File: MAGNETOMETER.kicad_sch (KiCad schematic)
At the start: 0 parts

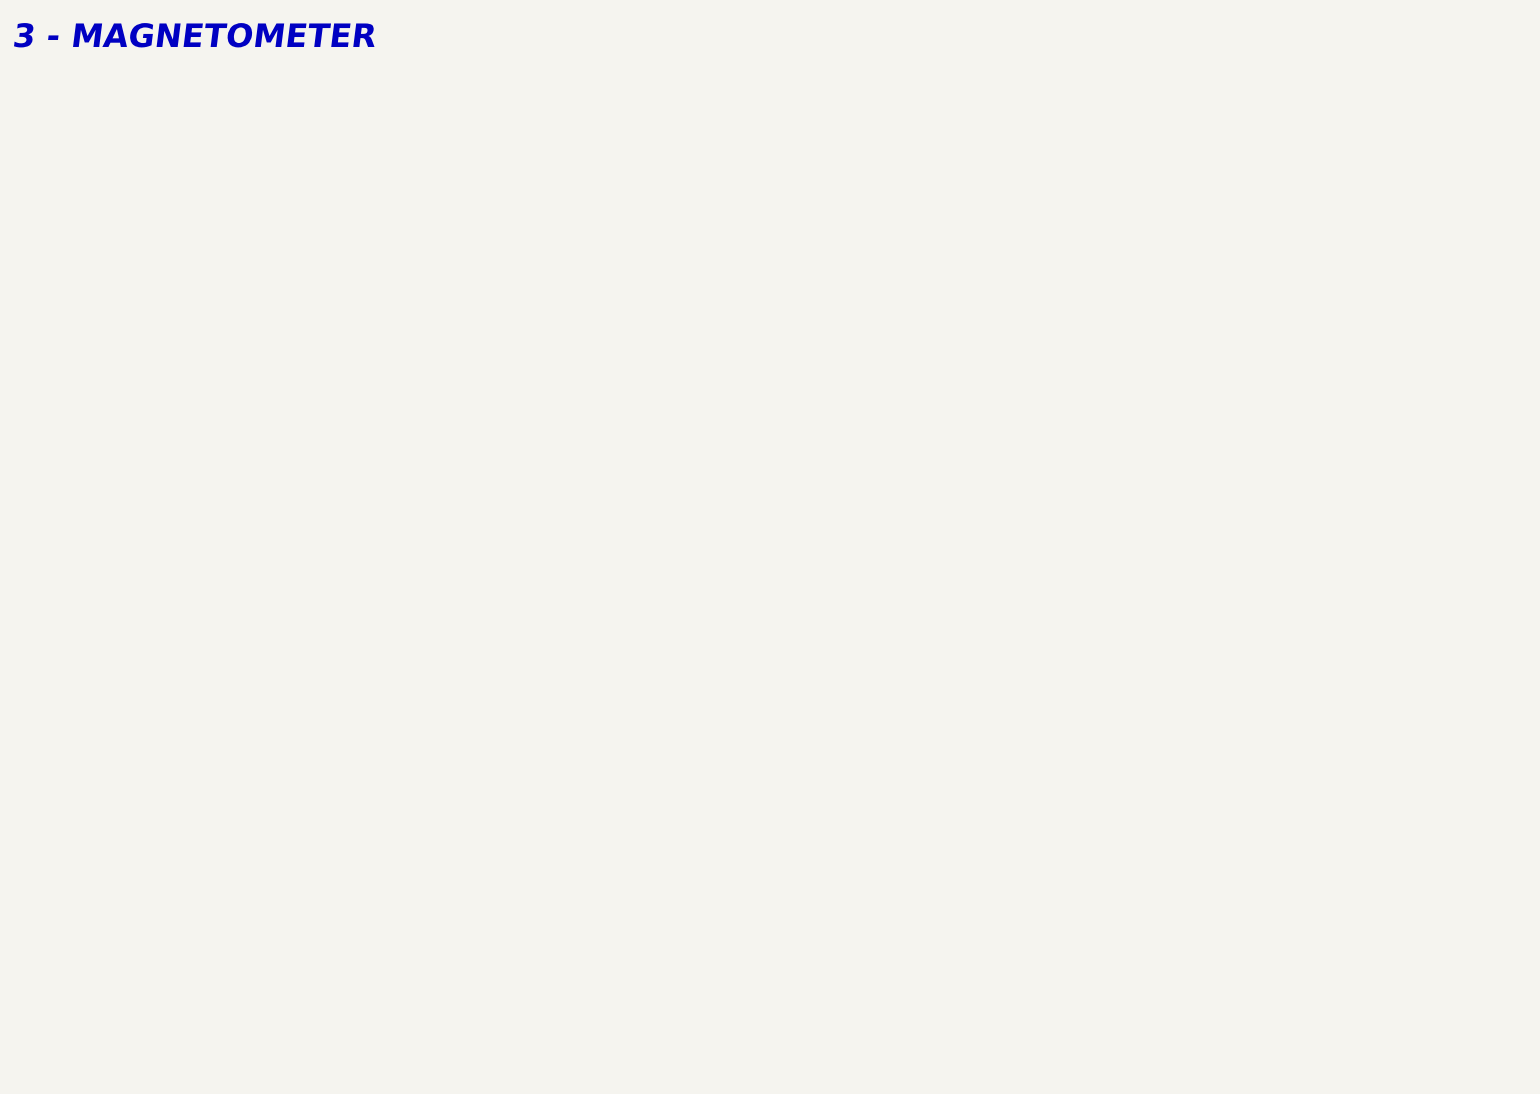
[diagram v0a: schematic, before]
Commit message: magnetometer design
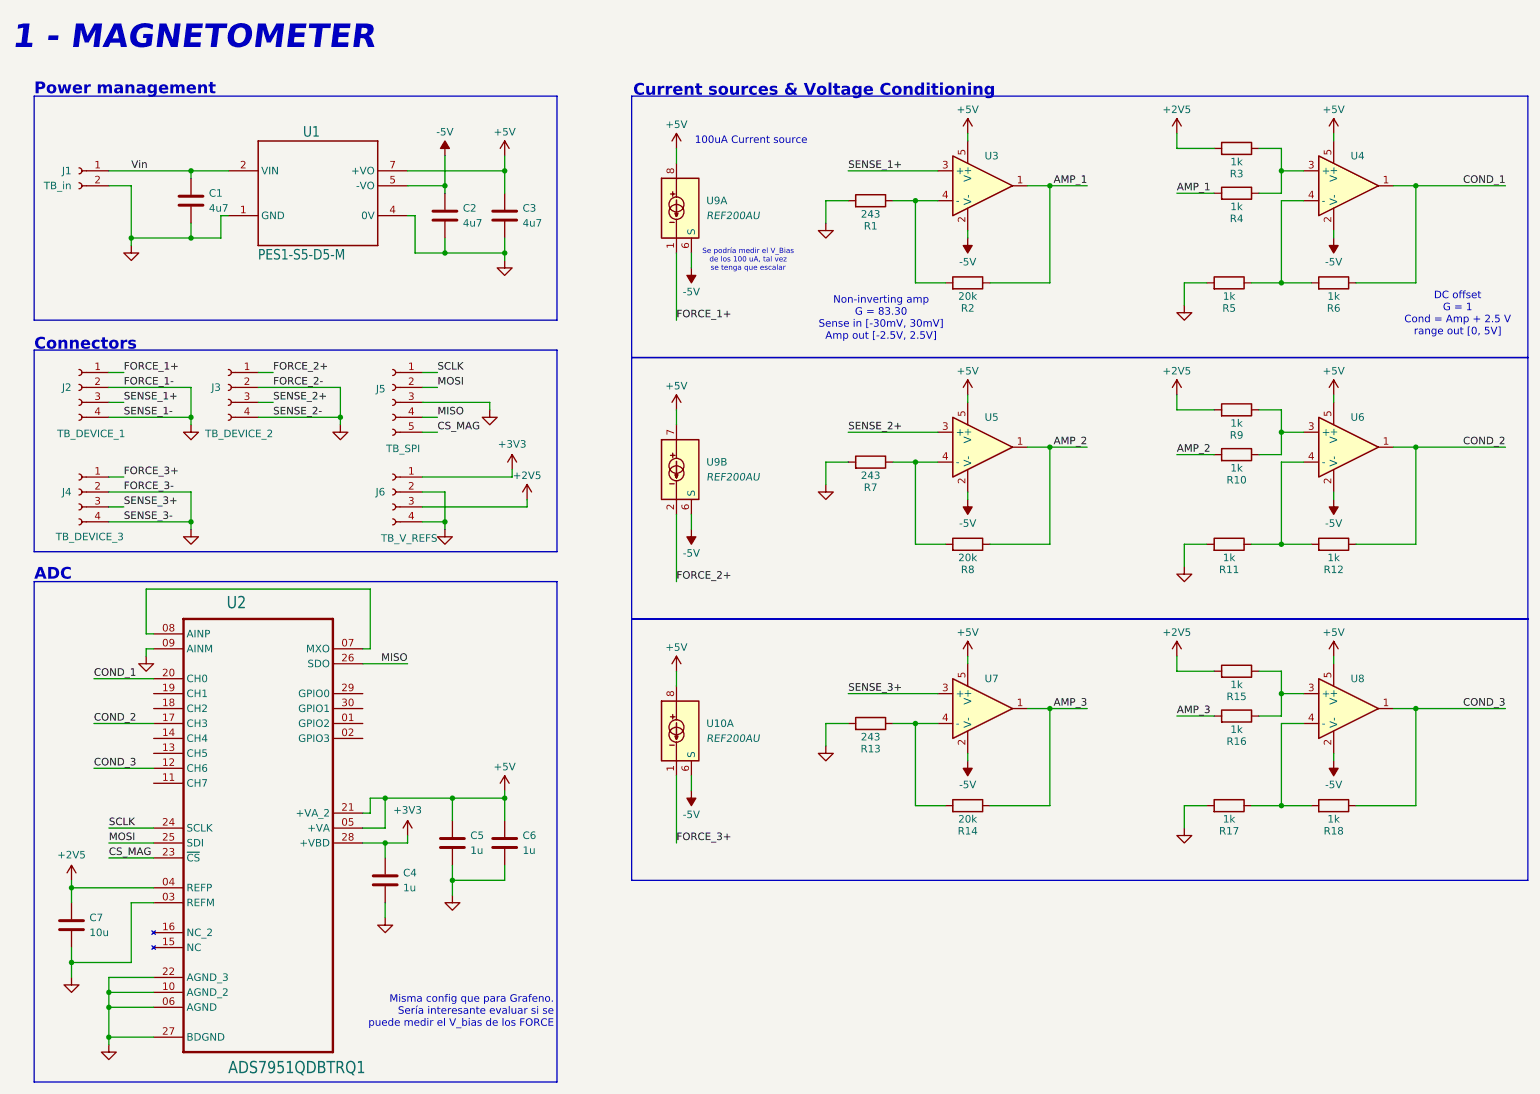
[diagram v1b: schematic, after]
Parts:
- added C1, C2, C3: 4u7, Capacitor_SMD:C_0805_2012Metric_Pad1.18x1.45mm_HandSolder, symbol Device:C
- added C4, C5, C6: 1u, Capacitor_SMD:C_0805_2012Metric_Pad1.18x1.45mm_HandSolder, symbol Device:C
- added C7: 10u, Capacitor_SMD:C_0805_2012Metric_Pad1.18x1.45mm_HandSolder, symbol Device:C
- added J1: TB_in, symbol Connector:Conn_01x02_Socket
- added J2: TB_DEVICE_1, symbol Connector:Conn_01x04_Socket
- added J3: TB_DEVICE_2, symbol Connector:Conn_01x04_Socket
- added J4: TB_DEVICE_3, symbol Connector:Conn_01x04_Socket
- added J5: TB_SPI, symbol Connector:Conn_01x05_Socket
- added J6: TB_V_REFS, symbol Connector:Conn_01x04_Socket
- added R1, R13, R7: 243, Resistor_SMD:R_0805_2012Metric_Pad1.20x1.40mm_HandSolder, symbol Device:R
- added R10, R11, R12, R15, R16, R17, R18, R3, R4, R5, R6, R9: 1k, Resistor_SMD:R_0805_2012Metric_Pad1.20x1.40mm_HandSolder, symbol Device:R
- added R14, R2, R8: 20k, Resistor_SMD:R_0805_2012Metric_Pad1.20x1.40mm_HandSolder, symbol Device:R
- added U1: PES1-S5-D5-M, TG_SAT_24V0_V1.4:CONV_PES1-S5-D24-M, symbol TG_SAT_24V0_V1.4-eagle-import:PES1-S5-D24-M
- added U10, U9: REF200AU, Package_SO:SOIC-8_3.9x4.9mm_P1.27mm, symbol Reference_Current:REF200AU
- added U2: ADS7951QDBTRQ1, Package_SO:TSSOP-30_4.4x7.8mm_P0.5mm, symbol TG_SAT_24V0_V1.4-eagle-import:ADS7951QDBTRQ1
- added U3, U4, U5, U6, U7, U8: ~, Package_TO_SOT_SMD:SOT-23-5_HandSoldering, symbol magnetometer_symbols:OPA189IDBVT
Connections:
- new net: R13.1, R14.2, U7.4 (-)
- new net: R3.1, R4.1, U4.3 (+)
- new net: R5.1, R6.2, U4.4 (-)
- new net: R10.1, R9.1, U6.3 (+)
- new net: R17.1, R18.2, U8.4 (-)
- new net: R11.1, R12.2, U6.4 (-)
- new net: U2.07 (MXO), U2.08 (AINP)
- new net: R7.1, R8.2, U5.4 (-)
- new net: R15.1, R16.1, U8.3 (+)
- new net: R1.1, R2.2, U3.4 (-)
- new net +2V5: C7.1, J6.3 (Pin_3), R15.2, R3.2, R9.2, U2.04 (REFP)
- new net +3V3: C4.1, J6.1 (Pin_1), U2.28 (+VBD)
- new net +5V: C3.1, C5.1, C6.1, U1.7 (+VO), U10.8, U2.05 (+VA), U2.21 (+VA_2), U3.5 (V+), U4.5 (V+), U5.5 (V+), U6.5 (V+), U7.5 (V+), U8.5 (V+), U9.7, U9.8
- new net -5V: C2.1, U1.5 (-VO), U10.6 (S), U3.2 (V-), U4.2 (V-), U5.2 (V-), U6.2 (V-), U7.2 (V-), U8.2 (V-), U9.6 (S), U9.6 (S)
- new net AMP_1: R2.1, R4.2, U3.1
- new net AMP_2: R10.2, R8.1, U5.1
- new net AMP_3: R14.1, R16.2, U7.1
- new net COND_1: R6.1, U2.20 (CH0), U4.1
- new net COND_2: R12.1, U2.17 (CH3), U6.1
- new net COND_3: R18.1, U2.12 (CH6), U8.1
- new net CS_MAG: J5.5 (Pin_5), U2.23 (~{CS})
- new net FORCE_1+: J2.1 (Pin_1), U9.1
- new net FORCE_2+: J3.1 (Pin_1), U9.2
- new net FORCE_3+: J4.1 (Pin_1), U10.1
- new net GND: C1.2, C2.2, C3.2, C4.2, C5.2, C6.2, C7.2, J1.2 (Pin_2), J2.2 (Pin_2), J2.4 (Pin_4), J3.2 (Pin_2), J3.4 (Pin_4), J4.2 (Pin_2), J4.4 (Pin_4), J5.3 (Pin_3), J6.2 (Pin_2), J6.4 (Pin_4), R1.2, R11.2, R13.2, R17.2, R5.2, R7.2, U1.1 (GND), U1.4 (0V), U2.03 (REFM), U2.06 (AGND), U2.09 (AINM), U2.10 (AGND_2), U2.22 (AGND_3), U2.27 (BDGND)
- new net MISO: J5.4 (Pin_4), U2.26 (SDO)
- new net MOSI: J5.2 (Pin_2), U2.25 (SDI)
- new net SCLK: J5.1 (Pin_1), U2.24 (SCLK)
- new net SENSE_1+: J2.3 (Pin_3), U3.3 (+)
- new net SENSE_2+: J3.3 (Pin_3), U5.3 (+)
- new net SENSE_3+: J4.3 (Pin_3), U7.3 (+)
- new net Vin: C1.1, J1.1 (Pin_1), U1.2 (VIN)
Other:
- note added: "1 - MAGNETOMETER"
- note added: "100uA Current source"
- note added: "ADC"
- note added: "Connectors"
- note added: "Current sources & Voltage Conditioning"
- note added: "DC offset G = 1 Cond = Amp + 2.5 V range out [0, 5V]"
- note added: "Misma config que para Grafeno. Sería interesante evaluar si se puede medir el V_bias de los FORCE"
- note added: "Non-inverting amp G = 83.30 Sense in [-30mV, 30mV] Amp out [-2.5V, 2.5V]"
- note added: "Power management"
- note added: "Se podría medir el V_Bias de los 100 uA, tal vez se tenga que escalar"
- note removed: "3 - MAGNETOMETER"
